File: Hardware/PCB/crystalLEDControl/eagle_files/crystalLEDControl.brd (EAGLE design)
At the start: 35 x 35 mm, 6 parts

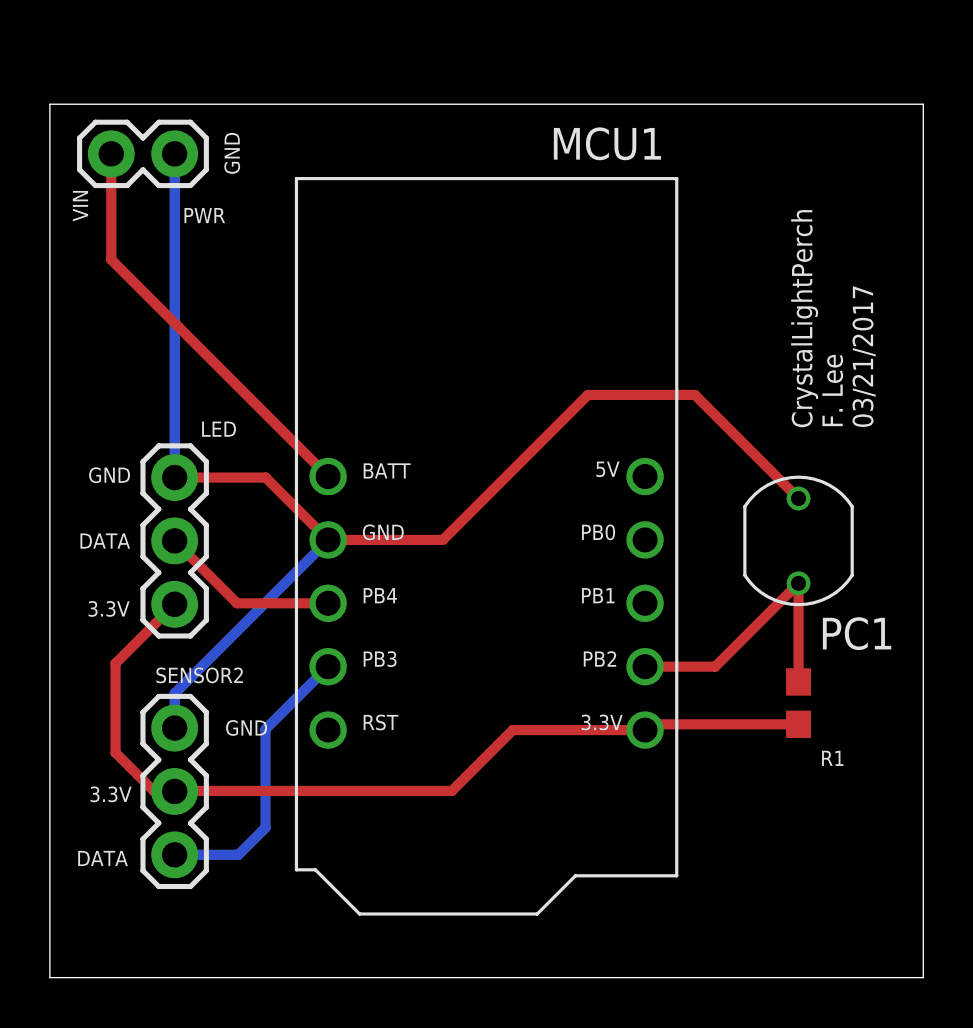
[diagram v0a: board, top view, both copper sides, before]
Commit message: Narrow board to fit better in 3D printed part.
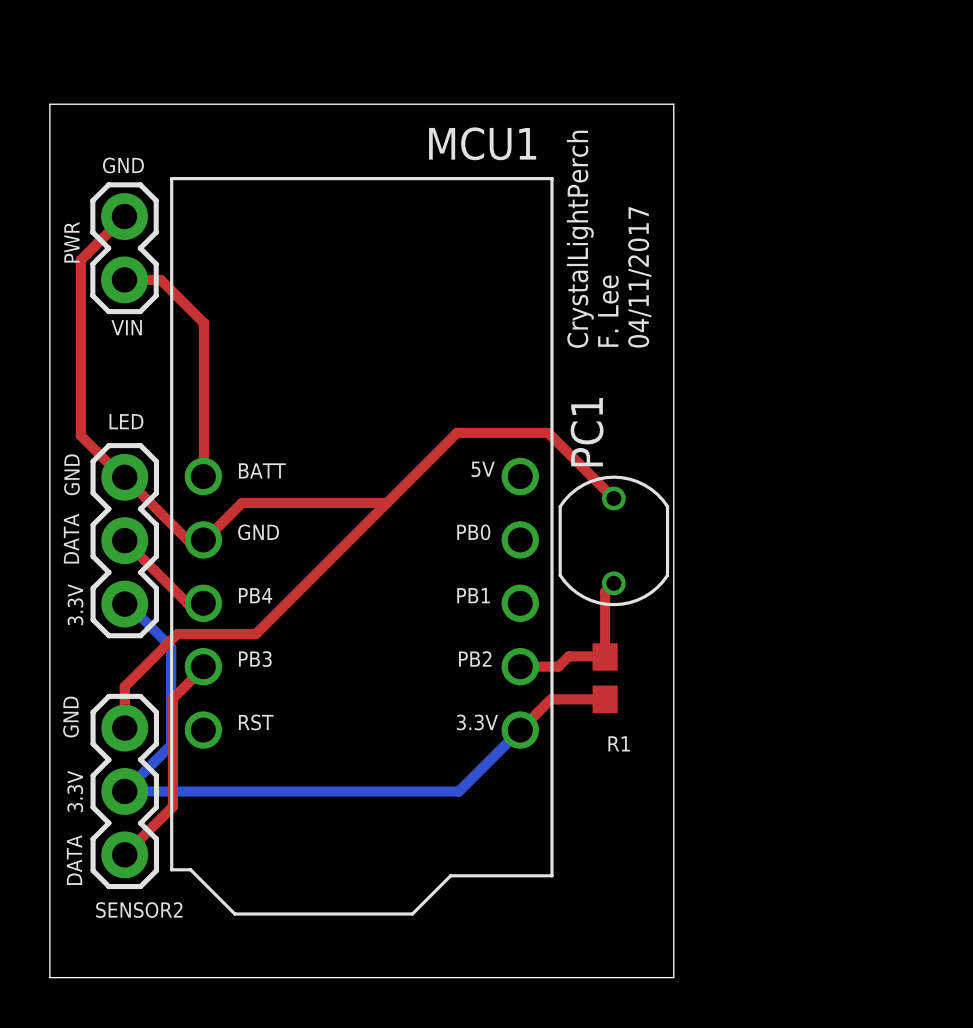
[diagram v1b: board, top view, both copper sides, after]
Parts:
- moved R1 7.81 mm to (22.2, 12.0)
- moved PC1 7.40 mm to (22.6, 17.5)
- moved MCU1 5.00 mm to (12.5, 15.0)
- moved PWR 3.22 mm to (2.99, 30.5), turned to 270 degrees
- moved LED 2.00 mm to (3.00, 15.0)
- moved SENSOR2 2.00 mm to (3.00, 10.0)
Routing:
- net VIN: track 16.5 -> 10.1 mm
- net 3.3V: track 36.1 -> 29.9 mm
- net LIGHT_SENSOR_IN: track 11.5 -> 6.67 mm
- net LED_DATA: track 7.19 -> 4.19 mm
- net SENSOR_EXP_IN: track 11.6 -> 8.84 mm
- net GND: track 53.2 -> 50.7 mm
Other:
- board size 35 x 35 mm -> 25 x 35 mm
- board text added: "CrystalLightPerch F. Lee 04/11/2017"
- board text removed: "CrystalLightPerch F. Lee 03/21/2017"

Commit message: Add MIMS microphone and support directly to board.
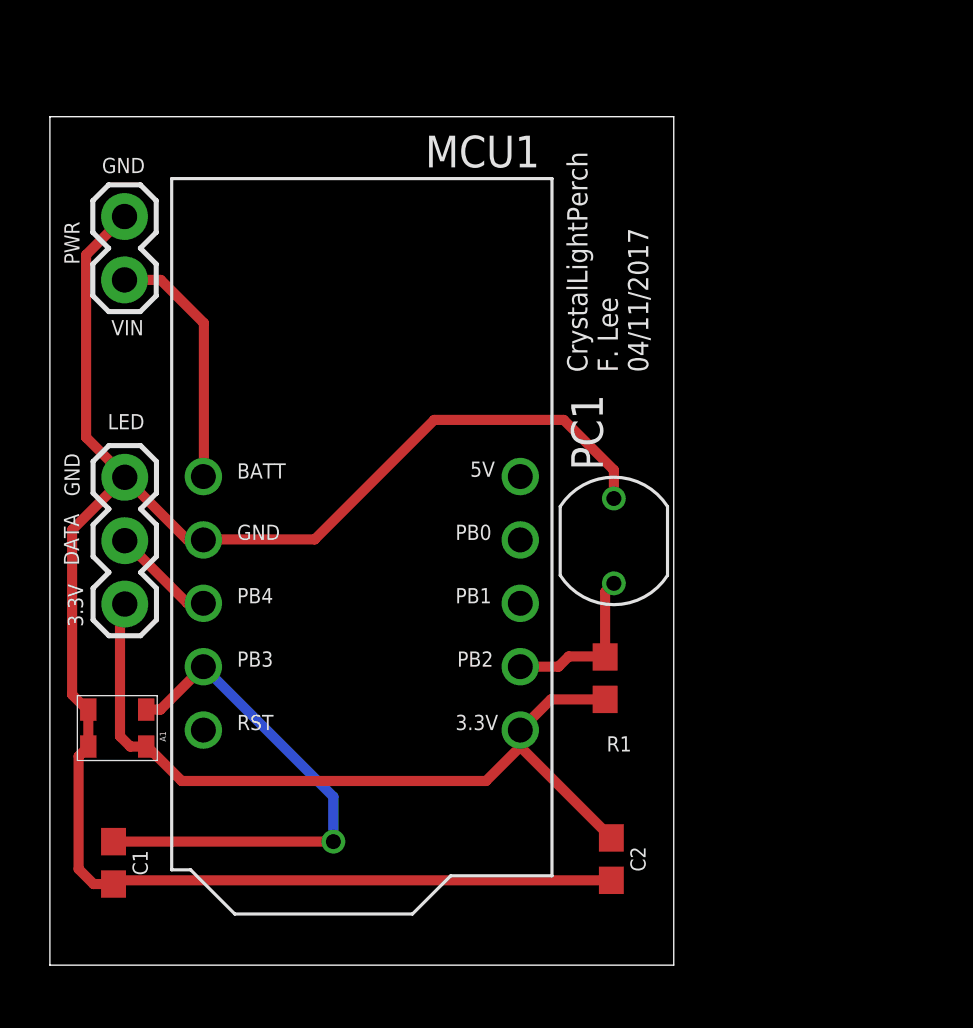
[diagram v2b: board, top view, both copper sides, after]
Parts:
- removed SENSOR2: (no value), SparkFun-Connectors:1X03
- added A1: (no value), freddyLibr:SPW2430
- added C1, C2: 4.7uF, SparkFun-Capacitors:0603
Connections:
- removed net SENSOR_EXP_IN: MCU1.PB3, SENSOR2.3
- new net MIC_IN: A1.OUT, C1.1, MCU1.PB3
- net 3.3V: now also A1.VCC, C2.1; no longer SENSOR2.2
- net GND: now also A1.GND1, A1.GND2, C1.2, C2.2; no longer SENSOR2.1
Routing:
- net GND: track 50.7 -> 75.0 mm
- net MIC_IN: track 0.00 -> 21.0 mm, vias 0 -> 1
- net SENSOR_EXP_IN: track 8.84 -> 0.00 mm
- net 3.3V: track 29.9 -> 32.5 mm
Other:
- board size 25 x 35 mm -> 25 x 34 mm
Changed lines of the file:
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@@
 <board>
 <plain>
-<wire x1="0" y1="0" x2="25" y2="0" width="0" layer="20"/>
-<wire x1="25" y1="0" x2="25" y2="35" width="0" layer="20"/>
-<wire x1="25" y1="35" x2="0" y2="35" width="0" layer="20"/>
-<wire x1="0" y1="35" x2="0" y2="0" width="0" layer="20"/>
-<text x="24" y="25.18" size="0.8128" layer="25" rot="R90">CrystalLightPerch
+<wire x1="0" y1="0.5" x2="25" y2="0.5" width="0" layer="20"/>
+<wire x1="25" y1="0.5" x2="25" y2="34.5" width="0" layer="20"/>
+<wire x1="25" y1="34.5" x2="0" y2="34.5" width="0" layer="20"/>
+<wire x1="0" y1="34.5" x2="0" y2="0.5" width="0" layer="20"/>
+<text x="23.98" y="24.26" size="0.8128" layer="25" rot="R90">CrystalLightPerch
 F. Lee
 04/11/2017</text>
-<text x="1.32" y="6.58" size="0.6096" layer="25" rot="R90">3.3V</text>
 <text x="1.33" y="14.06" size="0.6096" layer="25" rot="R90">3.3V</text>
 <text x="1.19" y="19.29" size="0.6096" layer="25" rot="R90">GND</text>
-<text x="1.15" y="9.58" size="0.6096" layer="25" rot="R90">GND</text>
 <text x="3.81" y="32.85" size="0.6096" layer="25" rot="R180">GND</text>
 <text x="3.76" y="26.35" size="0.6096" layer="25" rot="R180">VIN</text>
 <text x="1.17" y="16.52" size="0.6096" layer="25" rot="R90">DATA</text>
-<text x="1.29" y="3.64" size="0.6096" layer="25" rot="R90">DATA</text>
 </plain>
 <attributes>
@@
 <attribute name="VALUE" x="5.032" y="13.7" size="0.6096" layer="27" font="vector" ratio="20" rot="R90"/>
 </element>
-<element name="MCU1" library="trinketLib" package="ARDUINO_TRINKET" value="ARDUINO_TRINKET" x="12.5" y="15"/>
+<element name="MCU1" library="trinketLib" package="ARDUINO_TRINKET" value="ARDUINO_TRINKET" x="12.5" y="15" smashed="yes">
+<attribute name="NAME" x="15.04" y="32.47" size="1.27" layer="21"/>
+</element>
 <element name="PC1" library="freddyLibr" package="PHOTOCELL_CERAMIC" value="" x="22.6" y="17.5" smashed="yes" rot="R180">
 <attribute name="NAME" x="20.89" y="23.37" size="1.27" layer="25" rot="R270"/>
@@
 <attribute name="VALUE" x="21.212" y="8.96" size="0.6096" layer="27" font="vector" ratio="20" rot="R90" align="top-center"/>
 </element>
-<element name="SENSOR2" library="SparkFun-Connectors" package="1X03" value="" x="3" y="10" smashed="yes" rot="R270">
-<attribute name="NAME" x="5.39" y="3.013" size="0.6096" layer="25" font="vector" ratio="20" rot="R180"/>
-<attribute name="VALUE" x="0.968" y="11.27" size="0.6096" layer="27" font="vector" ratio="20" rot="R270"/>
+<element name="A1" library="freddyLibr" package="SPW2430" value="" x="2.7" y="10" rot="R270"/>
+<element name="C1" library="SparkFun-Capacitors" package="0603" value="4.7uF" x="2.55" y="4.6" rot="R270">
+<attribute name="PROD_ID" value="CAP-08280" x="2.55" y="4.6" size="1.778" layer="27" rot="R270" display="off"/>
+</element>
+<element name="C2" library="SparkFun-Capacitors" package="0603" value="4.7uF" x="22.5" y="4.75" rot="R270">
+<attribute name="PROD_ID" value="CAP-08280" x="22.5" y="4.75" size="1.778" layer="27" rot="R270" display="off"/>
 </element>
 </elements>
@@
 <contactref element="MCU1" pad="3.3V"/>
 <contactref element="R1" pad="2"/>
-<contactref element="SENSOR2" pad="2"/>
 <contactref element="LED" pad="1"/>
 <wire x1="22.25" y1="11.15" x2="20.08" y2="11.15" width="0.4064" layer="1"/>
 <wire x1="20.08" y1="11.15" x2="18.85" y2="9.92" width="0.4064" layer="1"/>
-<wire x1="3" y1="7.46" x2="16.39" y2="7.46" width="0.4064" layer="16"/>
-<wire x1="16.39" y1="7.46" x2="18.85" y2="9.92" width="0.4064" layer="16"/>
-<wire x1="3" y1="14.97" x2="3.13" y2="14.97" width="0.4064" layer="16"/>
-<wire x1="3.13" y1="14.97" x2="4.86" y2="13.24" width="0.4064" layer="16"/>
-<wire x1="4.86" y1="13.24" x2="4.86" y2="9.32" width="0.4064" layer="16"/>
-<wire x1="4.86" y1="9.32" x2="3" y2="7.46" width="0.4064" layer="16"/>
+<contactref element="A1" pad="VCC"/>
+<contactref element="C2" pad="1"/>
+<wire x1="18.85" y1="9.92" x2="18.85" y2="9.25" width="0.4064" layer="1"/>
+<wire x1="18.85" y1="9.25" x2="22.5" y2="5.6" width="0.4064" layer="1"/>
+<wire x1="3.86" y1="9.26" x2="3.9" y2="9.26" width="0.4064" layer="1"/>
+<wire x1="3.9" y1="9.26" x2="5.28" y2="7.88" width="0.4064" layer="1"/>
+<wire x1="5.28" y1="7.88" x2="17.48" y2="7.88" width="0.4064" layer="1"/>
+<wire x1="17.48" y1="7.88" x2="18.85" y2="9.25" width="0.4064" layer="1"/>
+<wire x1="3.86" y1="9.26" x2="3.22" y2="9.26" width="0.4064" layer="1"/>
+<wire x1="3.22" y1="9.26" x2="2.81" y2="9.67" width="0.4064" layer="1"/>
+<wire x1="2.81" y1="9.67" x2="2.81" y2="14.78" width="0.4064" layer="1"/>
+<wire x1="2.81" y1="14.78" x2="3" y2="14.97" width="0.4064" layer="1"/>
 </signal>
 <signal name="GND">
@@
 <contactref element="MCU1" pad="GND"/>
 <contactref element="PWR" pad="1"/>
-<contactref element="SENSOR2" pad="1"/>
 <contactref element="LED" pad="3"/>
 <wire x1="6.15" y1="17.54" x2="5.51" y2="17.54" width="0.4064" layer="1"/>
 <wire x1="5.51" y1="17.54" x2="3" y2="20.05" width="0.4064" layer="1"/>
-<wire x1="3" y1="20.05" x2="2.91" y2="20.05" width="0.4064" layer="1"/>
-<wire x1="2.91" y1="20.05" x2="1.24" y2="21.72" width="0.4064" layer="1"/>
-<wire x1="1.24" y1="21.72" x2="1.24" y2="28.75" width="0.4064" layer="1"/>
-<wire x1="1.24" y1="28.75" x2="2.99" y2="30.5" width="0.4064" layer="1"/>
-<wire x1="6.15" y1="17.54" x2="6.22" y2="17.54" width="0.4064" layer="1"/>
-<wire x1="6.22" y1="17.54" x2="7.7" y2="19.02" width="0.4064" layer="1"/>
-<wire x1="7.7" y1="19.02" x2="13.51" y2="19.02" width="0.4064" layer="1"/>
-<wire x1="13.51" y1="19.02" x2="16.32" y2="21.83" width="0.4064" layer="1"/>
-<wire x1="16.32" y1="21.83" x2="19.97" y2="21.83" width="0.4064" layer="1"/>
-<wire x1="19.97" y1="21.83" x2="22.6" y2="19.2" width="0.4064" layer="1"/>
-<wire x1="3" y1="10" x2="3" y2="11.66" width="0.4064" layer="1"/>
-<wire x1="3" y1="11.66" x2="5.11" y2="13.77" width="0.4064" layer="1"/>
-<wire x1="5.11" y1="13.77" x2="8.26" y2="13.77" width="0.4064" layer="1"/>
-<wire x1="8.26" y1="13.77" x2="13.51" y2="19.02" width="0.4064" layer="1"/>
+<contactref element="A1" pad="GND1"/>
+<contactref element="A1" pad="GND2"/>
+<contactref element="C1" pad="2"/>
+<contactref element="C2" pad="2"/>
+<wire x1="22.6" y1="19.2" x2="22.6" y2="20.34" width="0.4064" layer="1"/>
+<wire x1="22.6" y1="20.34" x2="20.59" y2="22.35" width="0.4064" layer="1"/>
+<wire x1="20.59" y1="22.35" x2="15.4" y2="22.35" width="0.4064" layer="1"/>
+<wire x1="15.4" y1="22.35" x2="10.61" y2="17.56" width="0.4064" layer="1"/>
+<wire x1="10.61" y1="17.56" x2="6.17" y2="17.56" width="0.4064" layer="1"/>
+<wire x1="6.17" y1="17.56" x2="6.15" y2="17.54" width="0.4064" layer="1"/>
+<wire x1="22.5" y1="3.9" x2="2.7" y2="3.9" width="0.4064" layer="1"/>
+<wire x1="2.7" y1="3.9" x2="2.55" y2="3.75" width="0.4064" layer="1"/>
+<wire x1="2.55" y1="3.75" x2="1.75" y2="3.75" width="0.4064" layer="1"/>
+<wire x1="1.75" y1="3.75" x2="1.15" y2="4.35" width="0.4064" layer="1"/>
+<wire x1="1.15" y1="4.35" x2="1.15" y2="8.87" width="0.4064" layer="1"/>
+<wire x1="1.15" y1="8.87" x2="1.54" y2="9.26" width="0.4064" layer="1"/>
+<wire x1="1.54" y1="9.26" x2="1.54" y2="10.74" width="0.4064" layer="1"/>
+<wire x1="1.54" y1="10.74" x2="1.49" y2="10.74" width="0.4064" layer="1"/>
+<wire x1="1.49" y1="10.74" x2="0.89" y2="11.34" width="0.4064" layer="1"/>
+<wire x1="0.89" y1="11.34" x2="0.89" y2="17.94" width="0.4064" layer="1"/>
+<wire x1="0.89" y1="17.94" x2="3" y2="20.05" width="0.4064" layer="1"/>
+<wire x1="3" y1="20.05" x2="3" y2="20.1" width="0.4064" layer="1"/>
+<wire x1="3" y1="20.1" x2="1.45" y2="21.65" width="0.4064" layer="1"/>
+<wire x1="1.45" y1="21.65" x2="1.45" y2="28.96" width="0.4064" layer="1"/>
+<wire x1="1.45" y1="28.96" x2="2.99" y2="30.5" width="0.4064" layer="1"/>
 </signal>
 <signal name="LED_DATA">
@@
 <wire x1="22.25" y1="15.45" x2="22.6" y2="15.8" width="0.4064" layer="1"/>
 </signal>
-<signal name="SENSOR_EXP_IN">
+<signal name="MIC_IN">
+<contactref element="A1" pad="OUT"/>
+<contactref element="C1" pad="1"/>
 <contactref element="MCU1" pad="PB3"/>
-<contactref element="SENSOR2" pad="3"/>
-<wire x1="6.15" y1="12.46" x2="6.15" y2="12.4" width="0.4064" layer="1"/>
-<wire x1="6.15" y1="12.4" x2="4.93" y2="11.18" width="0.4064" layer="1"/>
-<wire x1="4.93" y1="11.18" x2="4.93" y2="6.85" width="0.4064" layer="1"/>
-<wire x1="4.93" y1="6.85" x2="3" y2="4.92" width="0.4064" layer="1"/>
+<wire x1="3.86" y1="10.74" x2="4.43" y2="10.74" width="0.4064" layer="1"/>
+<wire x1="4.43" y1="10.74" x2="6.15" y2="12.46" width="0.4064" layer="1"/>
+<wire x1="2.55" y1="5.45" x2="11.36" y2="5.45" width="0.4064" layer="1"/>
+<via x="11.36" y="5.45" extent="1-16" drill="0.6"/>
+<wire x1="11.36" y1="5.45" x2="11.36" y2="7.25" width="0.4064" layer="16"/>
+<wire x1="11.36" y1="7.25" x2="6.15" y2="12.46" width="0.4064" layer="16"/>
 </signal>
 </signals>
